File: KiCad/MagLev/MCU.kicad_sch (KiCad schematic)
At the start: 5 parts, among them U6 ATmega328P-A, Y3 16MHz

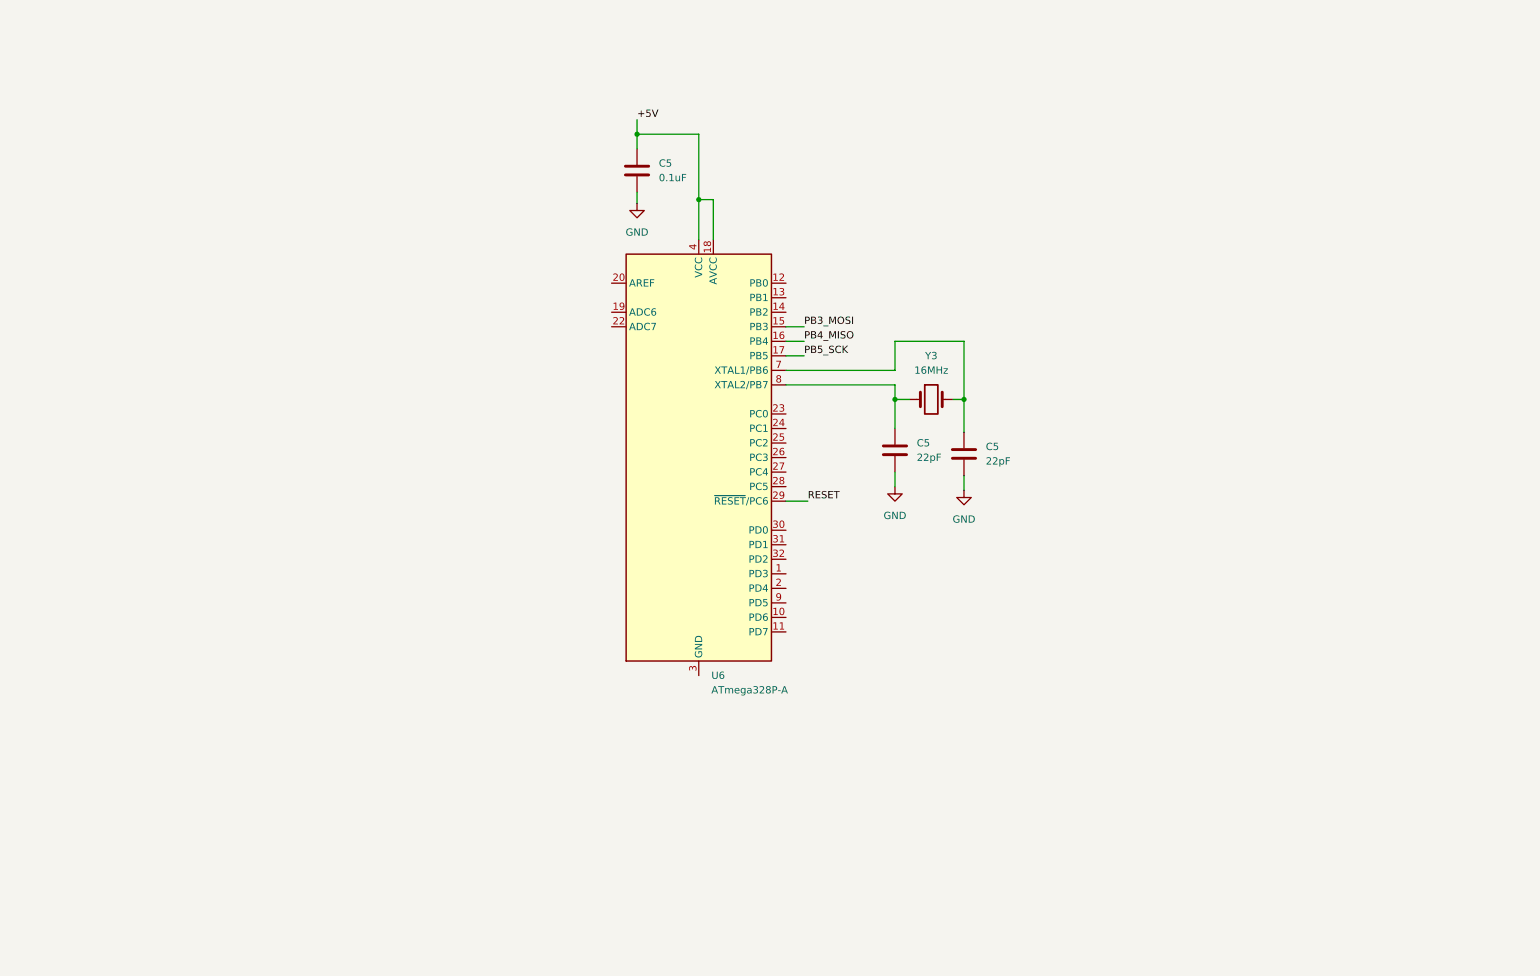
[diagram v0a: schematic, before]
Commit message: Add MCU and FTDI IC to schematic.
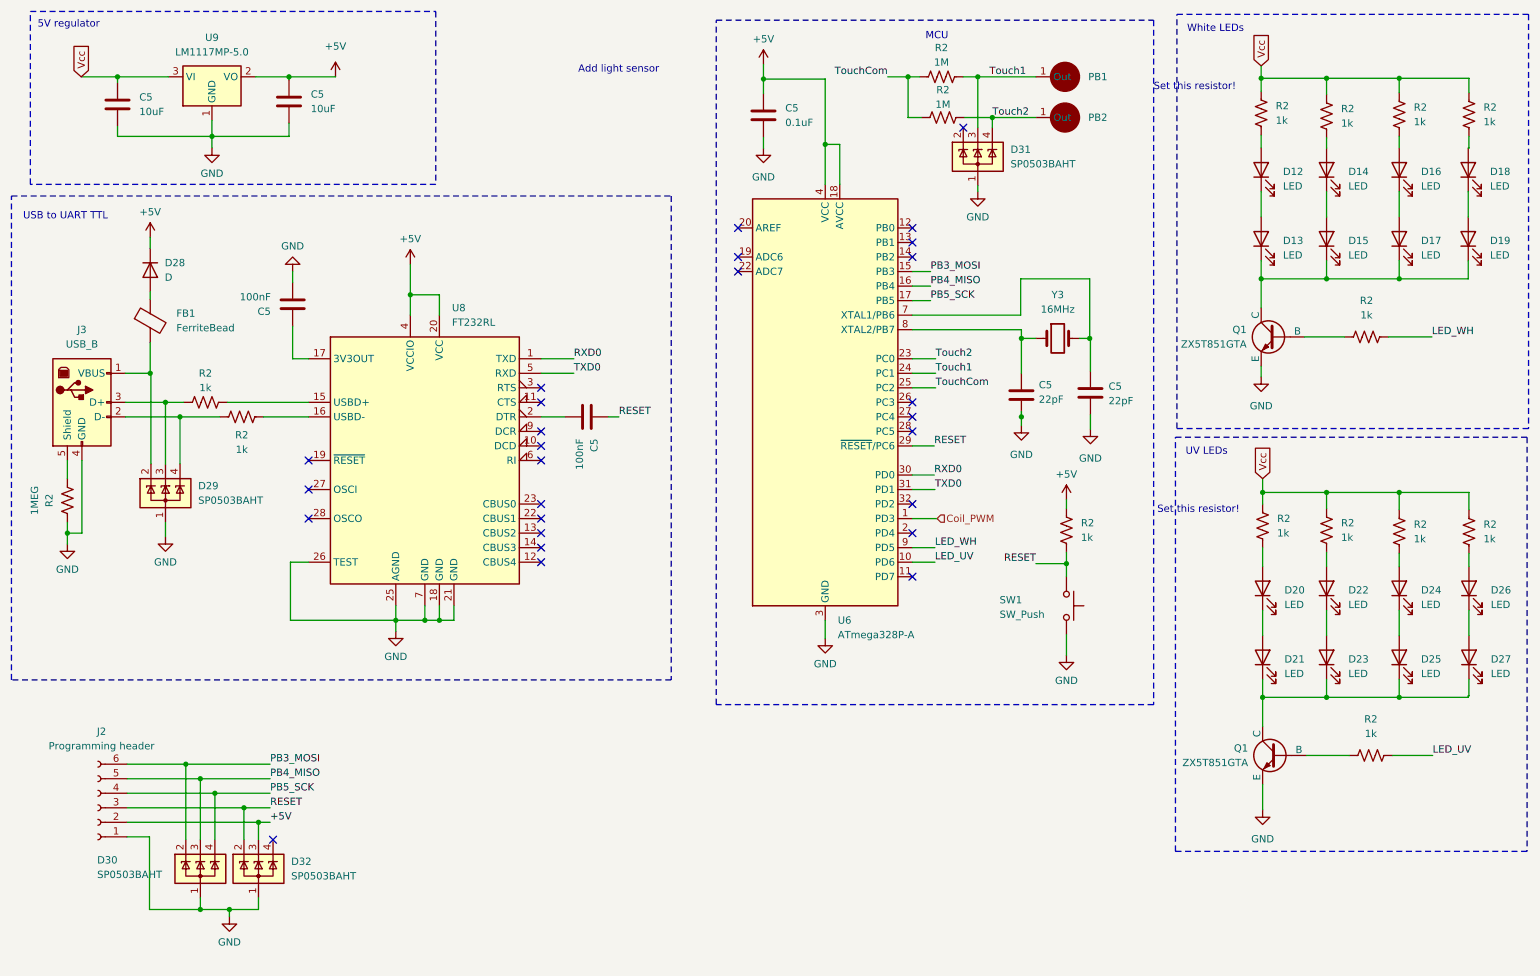
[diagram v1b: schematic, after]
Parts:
- added C5 (x2): 10uF, Capacitor_SMD:C_0805_2012Metric_Pad1.18x1.45mm_HandSolder, symbol Device:C
- added C5 (x2): 100nF, Capacitor_SMD:C_0805_2012Metric_Pad1.18x1.45mm_HandSolder, symbol Device:C
- added D12, D13, D14, D15, D16, D17, D18, D19, D20, D21, D22, D23, D24, D25, D26, D27: LED, symbol Device:LED
- added D28: D, symbol Device:D
- added D29, D30, D31, D32: SP0503BAHT, Package_TO_SOT_SMD:SOT-143, symbol Power_Protection:SP0503BAHT
- added FB1: FerriteBead, symbol Device:FerriteBead
- added J2: Programming header, symbol Connector:Conn_01x06_Socket
- added J3: USB_B, symbol Connector:USB_B
- added PB1, PB2: ~, symbol MagLev_Library:Cap_Touch
- added Q1 (x2): ZX5T851GTA, Maglev_Footprint_Library:SOT-223-3_TabPin2_BJT, symbol Simulation_SPICE:NPN
- added R2 (x13): 1k, Resistor_SMD:R_0805_2012Metric_Pad1.20x1.40mm_HandSolder, symbol Device:R_US
- added R2 (x2): 1M, Resistor_SMD:R_0805_2012Metric_Pad1.20x1.40mm_HandSolder, symbol Device:R_US
- added R2: 1MEG, Resistor_SMD:R_0805_2012Metric_Pad1.20x1.40mm_HandSolder, symbol Device:R_US
- added SW1: SW_Push, symbol Switch:SW_Push
- added U8: FT232RL, Package_SO:SSOP-28_5.3x10.2mm_P0.65mm, symbol Interface_USB:FT232RL
- added U9: LM1117MP-5.0, Package_TO_SOT_SMD:SOT-223-3_TabPin2, symbol Regulator_Linear:LM1117MP-5.0
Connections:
- net +5V: now also C5.1, D28.1 (K), D32.3 (K), J2.2 (Pin_2), R2.2, U8.20 (VCC), U8.4 (VCCIO), U9.2 (VO)
- net GND: now also U6.21 (GND), U6.3 (GND), U6.5 (GND), C5.2, C5.2, C5.2, D29.1 (A), D30.1 (A), D31.1 (A), D32.1 (A), J2.1 (Pin_1), J3.4 (GND), Q1.3 (E), Q1.3 (E), R2.1, SW1.2, U8.18 (GND), U8.21 (GND), U8.25 (AGND), U8.26 (TEST), U8.7 (GND), U9.1 (GND)
- net PB3_MOSI: now also D30.2 (K), J2.6 (Pin_6)
- net PB4_MISO: now also D30.3 (K), J2.5 (Pin_5)
- net PB5_SCK: now also D30.4 (K), J2.4 (Pin_4)
- net RESET: now also C5.1, D32.2 (K), J2.3 (Pin_3), R2.1, SW1.1
- net Coil_PWM: now reaches U6.1 (PD3)
- net LED_UV: now reaches U6.10 (PD6)
- net LED_UV: now also R2.2
- net Touch2: now reaches U6.23 (PC0)
- net Touch2: now also D31.4 (K), PB2.1 (Out), R2.1
- net Touch1: now reaches U6.24 (PC1)
- net Touch1: now also D31.3 (K), PB1.1 (Out), R2.1
- net TouchCom: now reaches U6.25 (PC2)
- net TouchCom: now also R2.2, R2.2
- net RXD0: now reaches U6.30 (PD0)
- net RXD0: now also U8.1 (TXD)
- net TXD0: now reaches U6.31 (PD1)
- net TXD0: now also U8.5 (RXD)
- net LED_WH: now reaches U6.9 (PD5)
- net LED_WH: now also R2.2
- new net: R2.2, U8.15 (USBD+)
- new net: R2.1, U8.16 (USBD-)
- new net: C5.1, U8.17 (3V3OUT)
- new net: C5.2, U8.2 (DTR)
- new net: D13.1 (K), D15.1 (K), D17.1 (K), D19.1 (K), Q1.1 (C)
- new net: Q1.2 (B), R2.1 (x2)
- new net: D22.2 (A), R2.1
- new net: D14.2 (A), R2.1
- new net: D16.1 (K), D17.2 (A)
- new net: D16.2 (A), R2.1
- new net: D22.1 (K), D23.2 (A)
- new net: D29.2 (K), FB1.2, J3.1 (VBUS)
- new net: D29.3 (K), J3.3 (D+), R2.1
- new net: D29.4 (K), J3.2 (D-), R2.2
- new net: D24.2 (A), R2.1
- new net: D20.1 (K), D21.2 (A)
- new net: D20.2 (A), R2.1
- new net: J3.5 (Shield), R2.2
- new net: D12.1 (K), D13.2 (A)
- new net: D14.1 (K), D15.2 (A)
- new net: D26.2 (A), R2.1
- new net: D28.2 (A), FB1.1
- new net: D12.2 (A), R2.1
- new net: D18.1 (K), D19.2 (A)
- new net: D18.2 (A), R2.1
- new net: D21.1 (K), D23.1 (K), D25.1 (K), D27.1 (K), Q1.1 (C)
- new net: D24.1 (K), D25.2 (A)
- new net: D26.1 (K), D27.2 (A)
- new net Vcc: C5.1, R2.2, R2.2, R2.2, R2.2, R2.2, R2.2, R2.2, R2.2, U9.3 (VI)
- no-connect marks 0 -> 27
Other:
- note added: "5V regulator"
- note added: "Add light sensor"
- note added: "MCU"
- note added: "Set this resistor!"
- note added: "USB to UART TTL"
- note added: "UV LEDs"
- note added: "White LEDs"
- moved on the sheet: C5, U6, Y3

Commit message: Add power fets and additional coils to schematic.
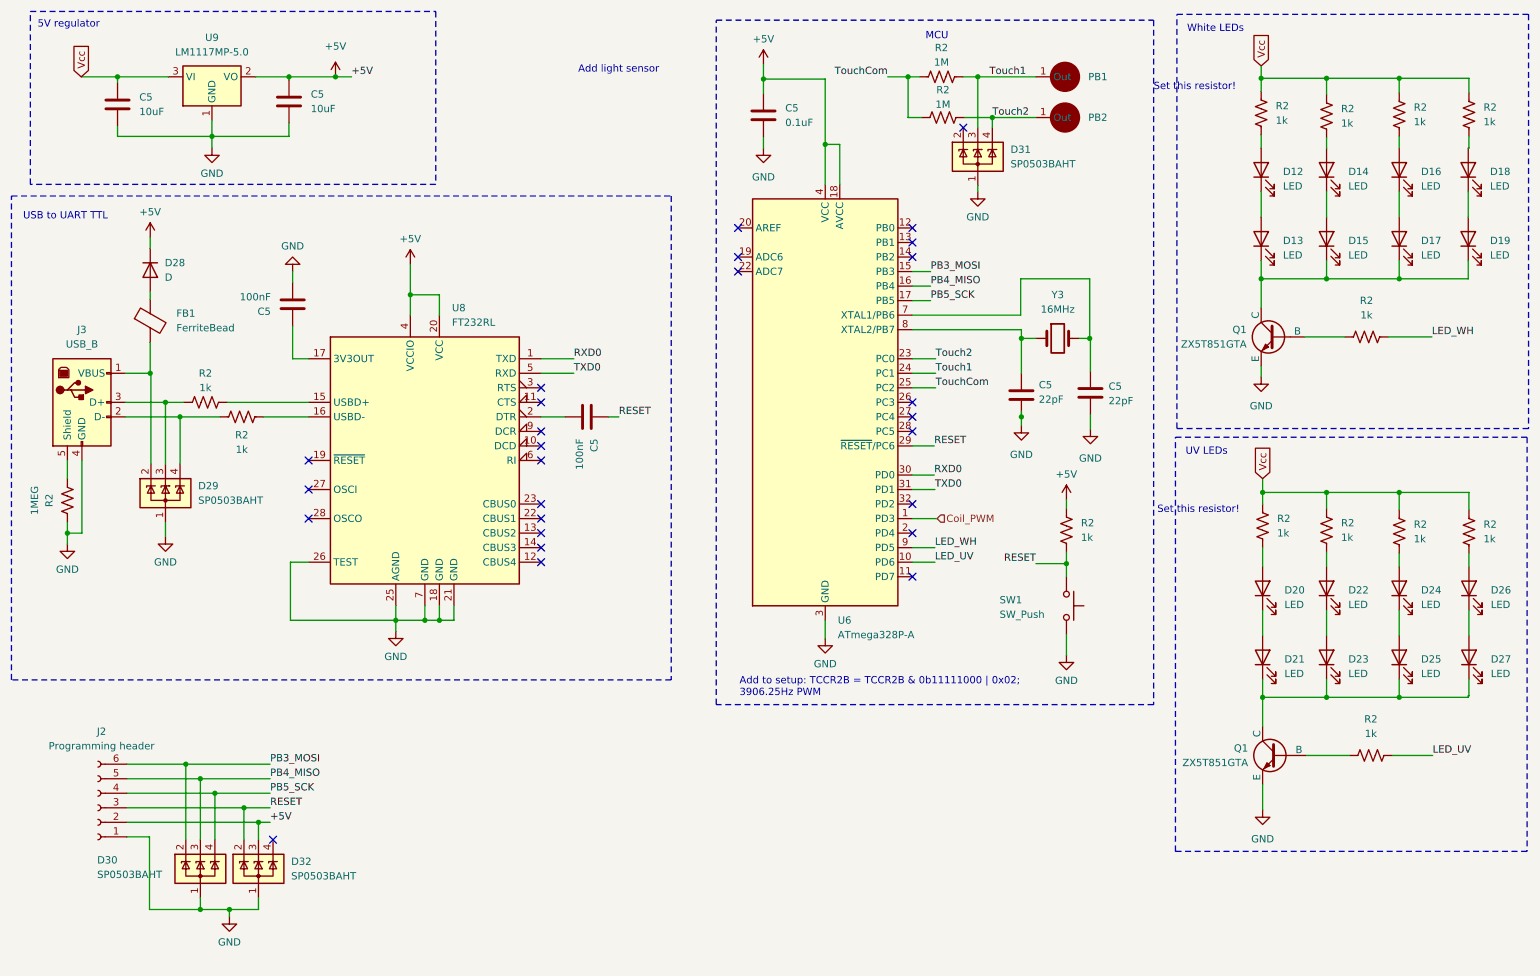
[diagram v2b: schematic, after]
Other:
- note added: "Add to setup: TCCR2B = TCCR2B & 0b11111000 | 0x02; 3906.25Hz PWM"
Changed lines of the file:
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@@
   (junction (at 52.07 37.846) (diameter 0) (color 0 0 0 0)
+  )
+  (junction (at 73.66 27.432) (diameter 0) (color 0 0 0 0)
   )
   (junction (at 50.038 172.974) (diameter 0) (color 0 0 0 0)
@@
     (stroke (width 0) (type default))
   )
+  (wire (pts (xy 73.66 27.432) (xy 76.454 27.432))
+    (stroke (width 0) (type default))
+  )
   (wire (pts (xy 89.281 122.428) (xy 84.201 122.428))
     (stroke (width 0) (type default))
@@
     (effects (font (size 1.27 1.27)) (justify left bottom))
   )
+  (text "Add to setup: TCCR2B = TCCR2B & 0b11111000 | 0x02;\n3906.25Hz PWM"
+    (at 144.272 135.89 0)
+    (effects (font (size 1.27 1.27)) (justify left bottom) (href "https://forum.arduino.cc/t/varying-the-pwm-frequency-for-timer-0-or-timer-2/16679/5"))
+  )
   (text "Set this resistor!" (at 216.662 29.972 0)
     (effects (font (size 1.27 1.27)) (justify left bottom))
@@
     (effects (font (size 1.27 1.27)) (justify left bottom))
   )
+  (label "+5V" (at 76.454 27.432 0) (fields_autoplaced)
+    (effects (font (size 1.27 1.27)) (justify left bottom))
+  )

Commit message: Add MCU enable circuit and leds.
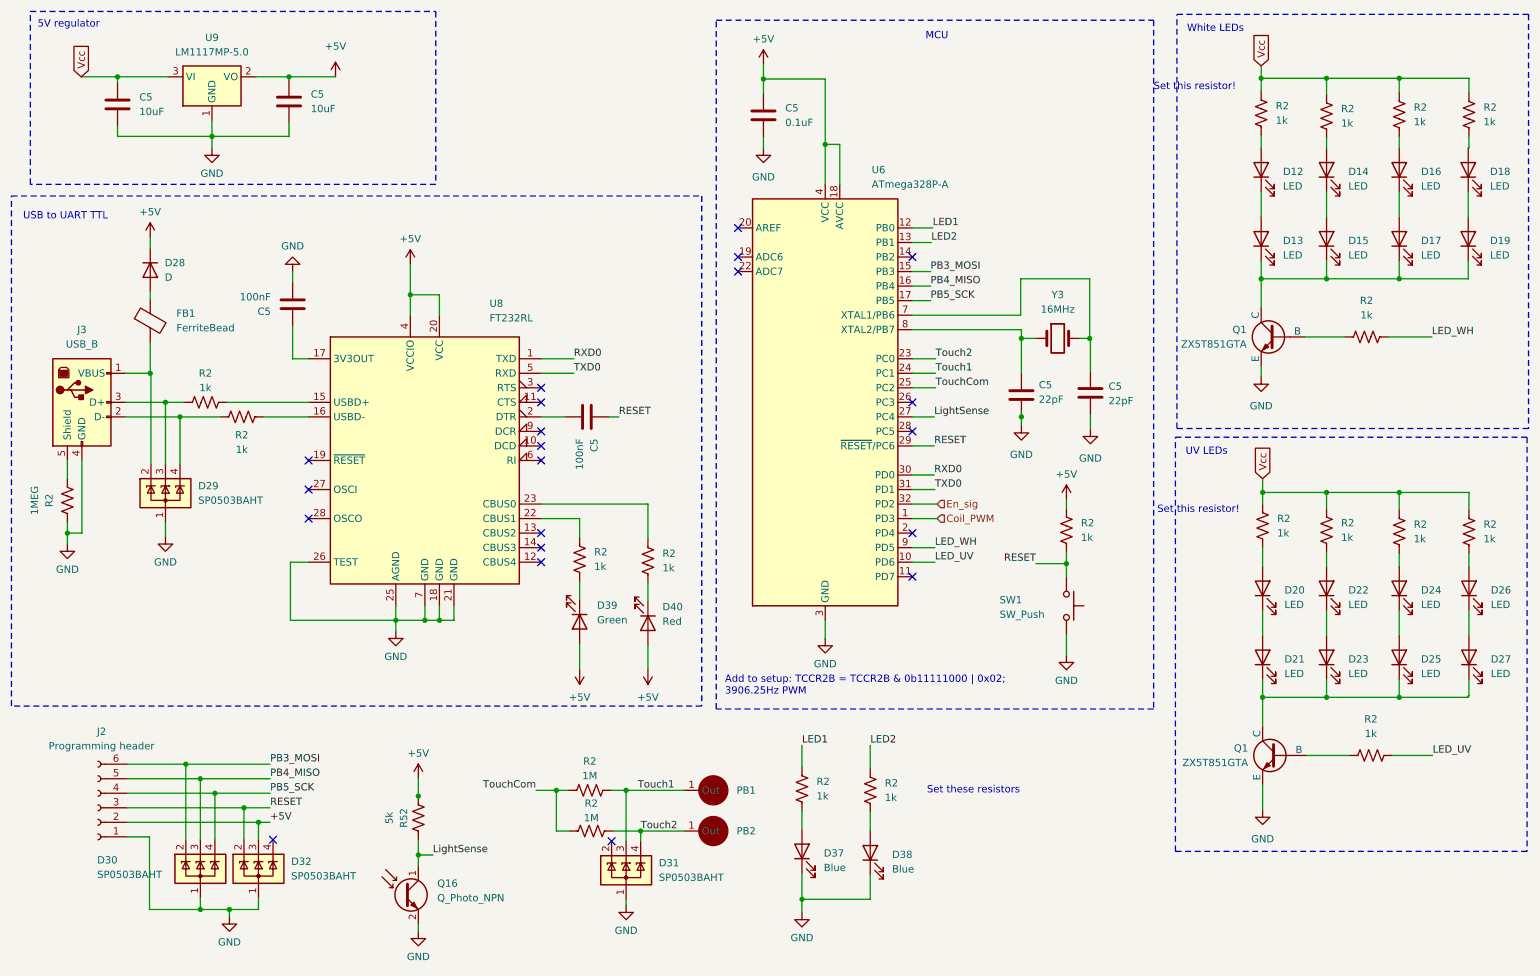
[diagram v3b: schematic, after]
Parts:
- added D37, D38: Blue, symbol Device:LED
- added D39: Green, symbol Device:LED
- added D40: Red, symbol Device:LED
- added Q16: Q_Photo_NPN, symbol Device:Q_Photo_NPN
- added R2 (x4): 1k, Resistor_SMD:R_0805_2012Metric_Pad1.20x1.40mm_HandSolder, symbol Device:R_US
- added R52: 5k, Resistor_SMD:R_0805_2012Metric_Pad1.20x1.40mm_HandSolder, symbol Device:R_US
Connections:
- net +5V: now also D39.2 (A), D40.2 (A), R52.1
- net GND: now also D37.1 (K), D38.1 (K), Q16.2 (E)
- net at U8.22 (CBUS1): now also R2.2
- net at U8.23 (CBUS0): now also R2.2
- net LED1: now reaches U6.12 (PB0)
- net LED1: now also R2.2
- net LED2: now reaches U6.13 (PB1)
- net LED2: now also R2.2
- net LightSense: now reaches U6.27 (PC4)
- net LightSense: now also Q16.1 (C)
- net En_sig: now reaches U6.32 (PD2)
- new net: D39.1 (K), R2.1
- new net: D38.2 (A), R2.1
- new net: D37.2 (A), R2.1
- new net: D40.1 (K), R2.1
- no-connect marks 27 -> 21
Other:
- note added: "Set these resistors"
- note removed: "Add light sensor"
- moved on the sheet: D31, PB1, PB2, R2

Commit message: Assign footprints to MCU components.
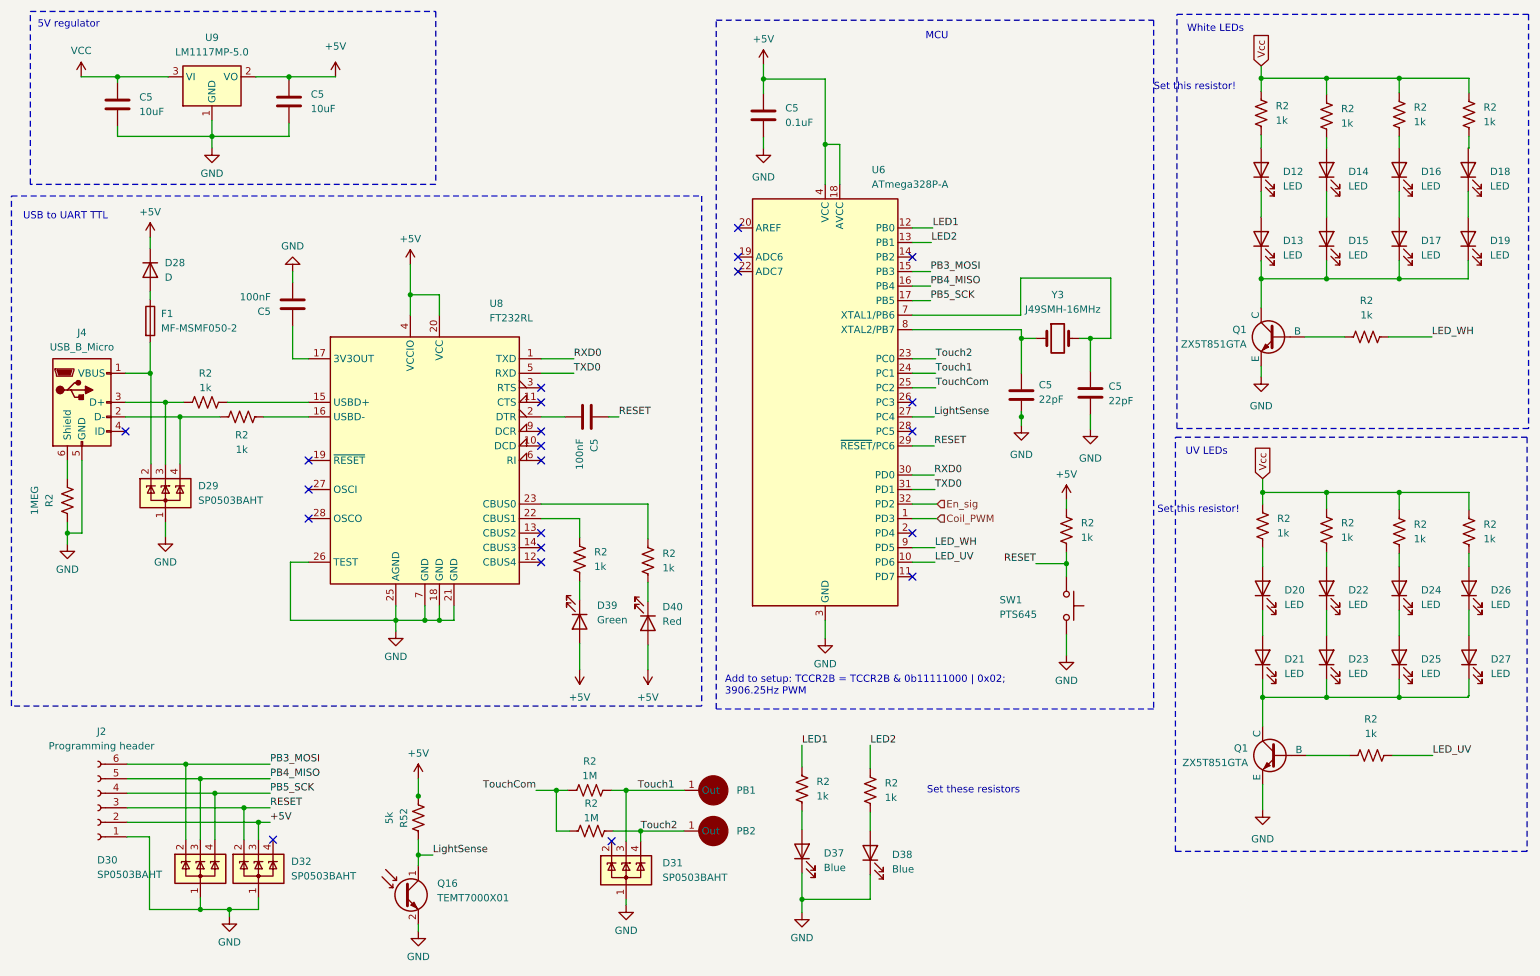
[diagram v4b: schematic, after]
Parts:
- removed FB1: FerriteBead, symbol Device:FerriteBead
- removed J3: USB_B, symbol Connector:USB_B
- added F1: MF-MSMF050-2, Fuse:Fuse_1812_4532Metric_Pad1.30x3.40mm_HandSolder, symbol Device:Fuse
- added J4: USB_B_Micro, Connector_USB:USB_Micro-B_Amphenol_10118193-0001LF_Horizontal, symbol Connector:USB_B_Micro
- D12, D13, D14, D15, D16, D17, D18, D19, D20, D21, D22, D23, D24, D25, D26, D27, D37, D38, D39, D40: footprint (none) -> LED_SMD:LED_0805_2012Metric_Pad1.15x1.40mm_HandSolder
- D28: footprint (none) -> Diode_SMD:D_SMA_Handsoldering
- J2: footprint (none) -> Maglev_Footprint_Library:PinSocket_1x06_P2.54mm_Horizontal_SM
- PB1, PB2: footprint (none) -> Maglev_Footprint_Library:Capacitive_Touch_Pad
- Q16: value Q_Photo_NPN -> TEMT7000X01; footprint (none) -> LED_SMD:LED_0805_2012Metric_Pad1.15x1.40mm_HandSolder
- SW1: value SW_Push -> PTS645; footprint (none) -> Button_Switch_SMD:SW_SPST_PTS645
- Y3: value 16MHz -> J49SMH-16MHz; footprint (none) -> Crystal:Crystal_SMD_HC49-SD_HandSoldering
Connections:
- net GND: now also J4.5 (GND)
- net LightSense: now also R52.2
- net Vcc: no longer C5.1, U9.3 (VI)
- net at D29.2 (K): now also F1.2, J4.1 (VBUS)
- net at D29.3 (K), R2.1: now also J4.3 (D+)
- net at D29.4 (K), R2.2: now also J4.2 (D-)
- net at R2.2: now also J4.6 (Shield)
- net at D28.2 (A): now also F1.1
- new net VCC: C5.1, U9.3 (VI)
- no-connect marks 21 -> 22
